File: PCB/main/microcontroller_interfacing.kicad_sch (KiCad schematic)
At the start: 14 parts, among them IC5 CP2102-GMR, U3 CAT24C256, U4 MICROXNJ

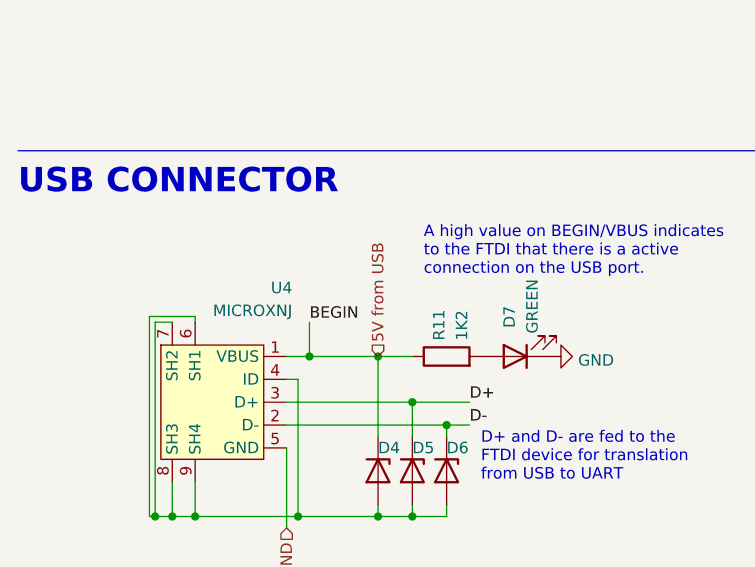
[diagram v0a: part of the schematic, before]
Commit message: Ran ERC and DRV
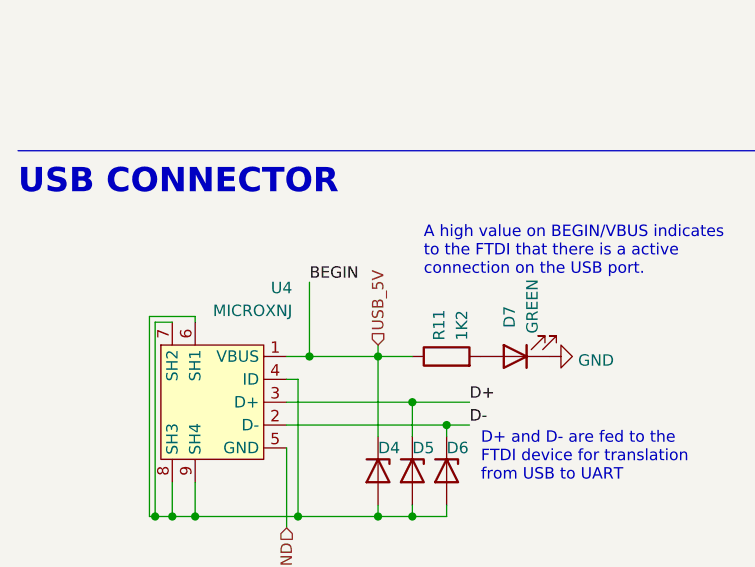
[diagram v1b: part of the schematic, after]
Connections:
- net 5V from USB renamed USB_5V
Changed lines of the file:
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@@
     (stroke (width 0) (type default) (color 0 0 0 0))
   )
-  (wire (pts (xy 45.085 97.79) (xy 45.085 101.6))
+  (wire (pts (xy 45.085 93.345) (xy 45.085 101.6))
     (stroke (width 0) (type default) (color 0 0 0 0))
   )
   (polyline (pts (xy 101.6 78.74) (xy 101.6 140.335))
+    (stroke (width 0) (type default) (color 0 0 0 0))
+  )
+  (wire (pts (xy 52.705 100.33) (xy 52.705 101.6))
     (stroke (width 0) (type default) (color 0 0 0 0))
   )
@@
     (effects (font (size 1.27 1.27)) (justify left bottom))
   )
-  (label "BEGIN" (at 45.085 97.79 0)
+  (label "BEGIN" (at 45.085 93.345 0)
     (effects (font (size 1.27 1.27)) (justify left bottom))
   )
@@
     (effects (font (size 1.27 1.27)) (justify left))
   )
-  (hierarchical_label "5V from USB" (shape input) (at 52.705 101.6 90)
+  (hierarchical_label "USB_5V" (shape input) (at 52.705 100.33 90)
     (effects (font (size 1.27 1.27)) (justify left))
   )

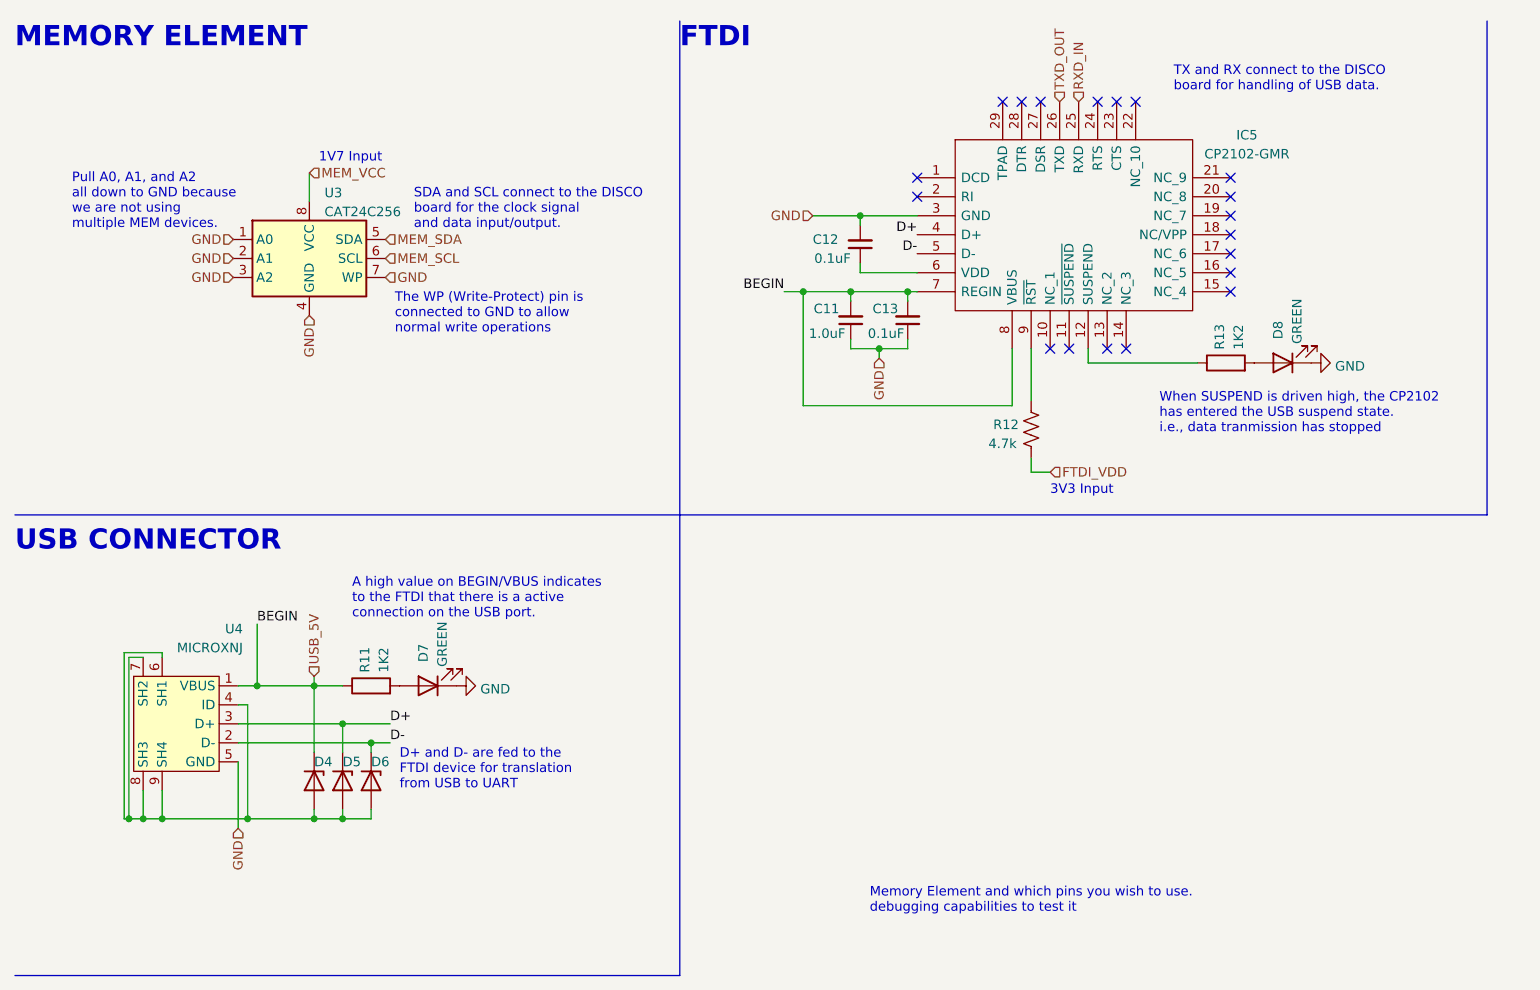
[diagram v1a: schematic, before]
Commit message: Updated MC Interfacing with pullups
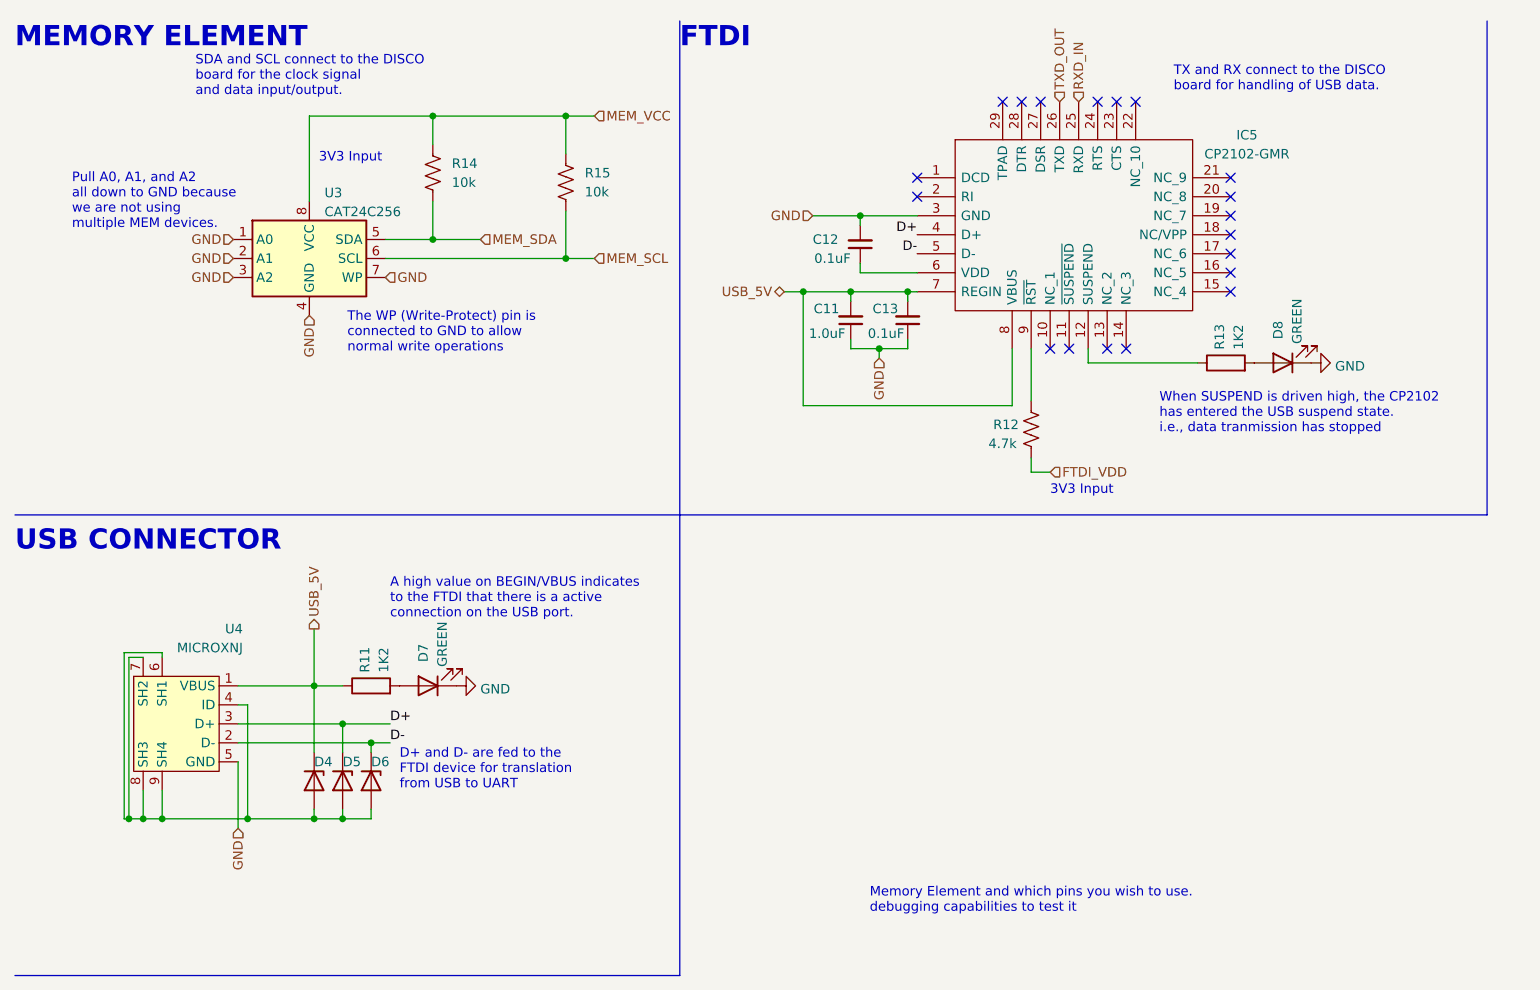
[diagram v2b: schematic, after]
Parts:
- added R14, R15: 10k, EEE3088F_Footprints:R0603, symbol Device:R_US
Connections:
- net MEM_SCL: now also R15.2
- net MEM_SDA: now also R14.2
- net MEM_VCC: now also R14.1, R15.1
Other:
- note removed: "1V7 Input"
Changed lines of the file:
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@@
   (junction (at 128.27 56.515) (diameter 0) (color 0 0 0 0)
   )
+  (junction (at 86.36 25.4) (diameter 0) (color 0 0 0 0)
+  )
   (junction (at 124.46 48.895) (diameter 0) (color 0 0 0 0)
   )
@@
   (junction (at 29.845 119.38) (diameter 0) (color 0 0 0 0)
   )
-  (junction (at 45.085 101.6) (diameter 0) (color 0 0 0 0)
-  )
   (junction (at 132.08 48.895) (diameter 0) (color 0 0 0 0)
   )
   (junction (at 60.325 109.22) (diameter 0) (color 0 0 0 0)
   )
+  (junction (at 68.58 25.4) (diameter 0) (color 0 0 0 0)
+  )
   (junction (at 125.73 38.735) (diameter 0) (color 0 0 0 0)
   )
+  (junction (at 86.36 44.45) (diameter 0) (color 0 0 0 0)
+  )
   (junction (at 52.705 119.38) (diameter 0) (color 0 0 0 0)
   )
@@
   )
   (junction (at 32.385 119.38) (diameter 0) (color 0 0 0 0)
+  )
+  (junction (at 68.58 41.91) (diameter 0) (color 0 0 0 0)
   )
   (junction (at 56.515 119.38) (diameter 0) (color 0 0 0 0)
@@
     (stroke (width 0) (type default) (color 0 0 0 0))
   )
+  (wire (pts (xy 86.36 44.45) (xy 62.23 44.45))
+    (stroke (width 0) (type default) (color 0 0 0 0))
+  )
   (wire (pts (xy 52.705 118.11) (xy 52.705 119.38))
     (stroke (width 0) (type default) (color 0 0 0 0))
@@
     (stroke (width 0) (type default) (color 0 0 0 0))
   )
-  (wire (pts (xy 45.085 93.345) (xy 45.085 101.6))
+  (wire (pts (xy 90.17 44.45) (xy 86.36 44.45))
     (stroke (width 0) (type default) (color 0 0 0 0))
   )
@@
     (stroke (width 0) (type default) (color 0 0 0 0))
   )
-  (wire (pts (xy 52.705 100.33) (xy 52.705 101.6))
+  (wire (pts (xy 52.705 93.98) (xy 52.705 101.6))
     (stroke (width 0) (type default) (color 0 0 0 0))
   )
@@
     (stroke (width 0) (type default) (color 0 0 0 0))
   )
+  (wire (pts (xy 68.58 25.4) (xy 86.36 25.4))
+    (stroke (width 0) (type default) (color 0 0 0 0))
+  )
+  (wire (pts (xy 86.36 25.4) (xy 90.17 25.4))
+    (stroke (width 0) (type default) (color 0 0 0 0))
+  )
   (polyline (pts (xy 209.55 78.74) (xy 101.6 78.74))
     (stroke (width 0) (type default) (color 0 0 0 0))
@@
     (stroke (width 0) (type default) (color 0 0 0 0))
   )
-  (wire (pts (xy 42.545 101.6) (xy 45.085 101.6))
+  (wire (pts (xy 74.93 41.91) (xy 68.58 41.91))
     (stroke (width 0) (type default) (color 0 0 0 0))
   )
@@
     (stroke (width 0) (type default) (color 0 0 0 0))
   )
+  (wire (pts (xy 86.36 38.1) (xy 86.36 44.45))
+    (stroke (width 0) (type default) (color 0 0 0 0))
+  )
   (wire (pts (xy 52.705 119.38) (xy 56.515 119.38))
     (stroke (width 0) (type default) (color 0 0 0 0))
@@
     (stroke (width 0) (type default) (color 0 0 0 0))
   )
+  (wire (pts (xy 68.58 25.4) (xy 68.58 29.21))
+    (stroke (width 0) (type default) (color 0 0 0 0))
+  )
   (wire (pts (xy 43.815 104.14) (xy 43.815 119.38))
     (stroke (width 0) (type default) (color 0 0 0 0))
   )
+  (wire (pts (xy 52.07 25.4) (xy 68.58 25.4))
+    (stroke (width 0) (type default) (color 0 0 0 0))
+  )
   (wire (pts (xy 148.59 71.12) (xy 148.59 73.025))
     (stroke (width 0) (type default) (color 0 0 0 0))
@@
     (stroke (width 0) (type default) (color 0 0 0 0))
   )
+  (wire (pts (xy 86.36 25.4) (xy 86.36 30.48))
+    (stroke (width 0) (type default) (color 0 0 0 0))
+  )
   (wire (pts (xy 148.59 56.515) (xy 148.59 63.5))
     (stroke (width 0) (type default) (color 0 0 0 0))
@@
     (stroke (width 0) (type default) (color 0 0 0 0))
   )
-  (wire (pts (xy 52.07 33.02) (xy 52.07 36.83))
+  (wire (pts (xy 52.07 25.4) (xy 52.07 36.83))
     (stroke (width 0) (type default) (color 0 0 0 0))
   )
@@
     (stroke (width 0) (type default) (color 0 0 0 0))
   )
+  (wire (pts (xy 68.58 41.91) (xy 62.23 41.91))
+    (stroke (width 0) (type default) (color 0 0 0 0))
+  )
   (wire (pts (xy 56.515 119.38) (xy 60.325 119.38))
     (stroke (width 0) (type default) (color 0 0 0 0))
@@
     (stroke (width 0) (type default) (color 0 0 0 0))
   )
-  (wire (pts (xy 45.085 101.6) (xy 52.705 101.6))
+  (wire (pts (xy 42.545 101.6) (xy 52.705 101.6))
     (stroke (width 0) (type default) (color 0 0 0 0))
   )
@@
     (stroke (width 0) (type default) (color 0 0 0 0))
   )
+  (wire (pts (xy 68.58 36.83) (xy 68.58 41.91))
+    (stroke (width 0) (type default) (color 0 0 0 0))
+  )
   (wire (pts (xy 43.815 119.38) (xy 52.705 119.38))
     (stroke (width 0) (type default) (color 0 0 0 0))
@@
     (stroke (width 0) (type default) (color 0 0 0 0))
   )
-  (text "1V7 Input\n" (at 53.34 31.75 0)
+  (text "3V3 Input\n" (at 53.34 31.75 0)
     (effects (font (size 1.27 1.27)) (justify left bottom))
   )
   (text "SDA and SCL connect to the DISCO\nboard for the clock signal\nand data input/output."
-    (at 66.04 40.64 0)
+    (at 36.83 22.86 0)
     (effects (font (size 1.27 1.27)) (justify left bottom))
   )
@@
   )
   (text "The WP (Write-Protect) pin is\nconnected to GND to allow \nnormal write operations"
-    (at 63.5 54.61 0)
+    (at 57.15 57.15 0)
     (effects (font (size 1.27 1.27)) (justify left bottom))
   )
@@
   )
   (text "A high value on BEGIN/VBUS indicates\nto the FTDI that there is a active\nconnection on the USB port.\n"
-    (at 57.785 92.71 0)
+    (at 62.865 92.71 0)
     (effects (font (size 1.27 1.27)) (justify left bottom))
   )
@@
     (effects (font (size 1.27 1.27)) (justify left bottom))
   )
-  (label "BEGIN" (at 45.085 93.345 0)
-    (effects (font (size 1.27 1.27)) (justify left bottom))
-  )
   (label "D+" (at 133.35 41.275 180)
     (effects (font (size 1.27 1.27)) (justify right bottom))
@@
     (effects (font (size 1.27 1.27)) (justify left bottom))
   )
-  (label "BEGIN" (at 115.57 48.895 180)
-    (effects (font (size 1.27 1.27)) (justify right bottom))
-  )
   (hierarchical_label "GND" (shape input) (at 42.545 120.65 270)
     (effects (font (size 1.27 1.27)) (justify right))
@@
     (effects (font (size 1.27 1.27)) (justify right))
   )
-  (hierarchical_label "MEM_SCL" (shape input) (at 62.23 44.45 0)
+  (hierarchical_label "MEM_SCL" (shape input) (at 90.17 44.45 0)
     (effects (font (size 1.27 1.27)) (justify left))
   )
@@
     (effects (font (size 1.27 1.27)) (justify left))
   )
-  (hierarchical_label "USB_5V" (shape input) (at 52.705 100.33 90)
+  (hierarchical_label "MEM_VCC" (shape input) (at 90.17 25.4 0)
     (effects (font (size 1.27 1.27)) (justify left))
   )
@@
     (effects (font (size 1.27 1.27)) (justify left))
   )
-  (hierarchical_label "MEM_SDA" (shape input) (at 62.23 41.91 0)
+  (hierarchical_label "MEM_SDA" (shape input) (at 74.93 41.91 0)
     (effects (font (size 1.27 1.27)) (justify left))
   )
@@
     (effects (font (size 1.27 1.27)) (justify right))
   )
-  (hierarchical_label "MEM_VCC" (shape input) (at 52.07 33.02 0)
-    (effects (font (size 1.27 1.27)) (justify left))
+  (hierarchical_label "USB_5V" (shape bidirectional) (at 115.57 48.895 180)
+    (effects (font (size 1.27 1.27)) (justify right))
   )
   (hierarchical_label "GND" (shape input) (at 52.07 52.07 270)
@@
   )
   (hierarchical_label "TXD_OUT" (shape input) (at 152.4 23.495 90)
+    (effects (font (size 1.27 1.27)) (justify left))
+  )
+  (hierarchical_label "USB_5V" (shape output) (at 52.705 93.98 90)
     (effects (font (size 1.27 1.27)) (justify left))
   )
@@
     (pin "2")
   )
+  (symbol (lib_id "Device:R_US") (at 68.58 33.02 0) (unit 1)
+    (in_bom yes) (on_board yes) (fields_autoplaced)
+    (property "Reference" "R14" (id 0) (at 71.12 31.7499 0)
+      (effects (font (size 1.27 1.27)) (justify left))
+    )
+    (property "Value" "10k" (id 1) (at 71.12 34.2899 0)
+      (effects (font (size 1.27 1.27)) (justify left))
+    )
+    (property "Footprint" "EEE3088F_Footprints:R0603" (id 2) (at 69.596 33.274 90)
+      (effects (font (size 1.27 1.27)) hide)
+    )
+    (property "Datasheet" "~" (id 3) (at 68.58 33.02 0)
+      (effects (font (size 1.27 1.27)) hide)
+    )
+    (pin "1")
+    (pin "2")
+  )
   (symbol (lib_id "Device:C_Small") (at 124.46 52.705 0) (mirror x) (unit 1)
     (in_bom yes) (on_board yes)
@@
       (effects (font (size 1.27 1.27)) hide)
     )
+    (pin "1")
+    (pin "2")
+  )
+  (symbol (lib_id "Device:R_US") (at 86.36 34.29 0) (unit 1)
+    (in_bom yes) (on_board yes) (fields_autoplaced)
+    (property "Reference" "R15" (id 0) (at 88.9 33.0199 0)
+      (effects (font (size 1.27 1.27)) (justify left))
+    )
+    (property "Value" "10k" (id 1) (at 88.9 35.5599 0)
+      (effects (font (size 1.27 1.27)) (justify left))
+    )
+    (property "Footprint" "EEE3088F_Footprints:R0603" (id 2) (at 87.376 34.544 90)
+      (effects (font (size 1.27 1.27)) hide)
+    )
+    (property "Datasheet" "~" (id 3) (at 86.36 34.29 0)
+      (effects (font (size 1.27 1.27)) hide)
+    )

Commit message: Added MCP6002 OpAmp files
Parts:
- U4: footprint EEE3088F_Footprints(new):MICRO-USB-SMD_MICROXNJ -> EEE3088F_Footprints:MICRO-USB-SMD_MICROXNJ
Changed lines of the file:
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@@
       (effects (font (size 1.27 1.27)) (justify right))
     )
-    (property "Footprint" "EEE3088F_Footprints(new):MICRO-USB-SMD_MICROXNJ" (id 2) (at 33.655 106.68 0)
+    (property "Footprint" "EEE3088F_Footprints:MICRO-USB-SMD_MICROXNJ" (id 2) (at 33.655 106.68 0)
       (effects (font (size 1.27 1.27)) hide)
     )
